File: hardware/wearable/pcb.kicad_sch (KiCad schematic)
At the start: 72 parts, among them IC1 LM4041CILPR, IC2 INA828IDR, IC3 MAX30102EFD+T, IC4 TPS63001DRCT, IC5 OPA2350UA, IC6 TPS62293DRVR, J1 Conn_02x05_Odd_Even, J2 Conn_01x04_Pin, SW1 SW_Push, SW2 SW_SPDT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

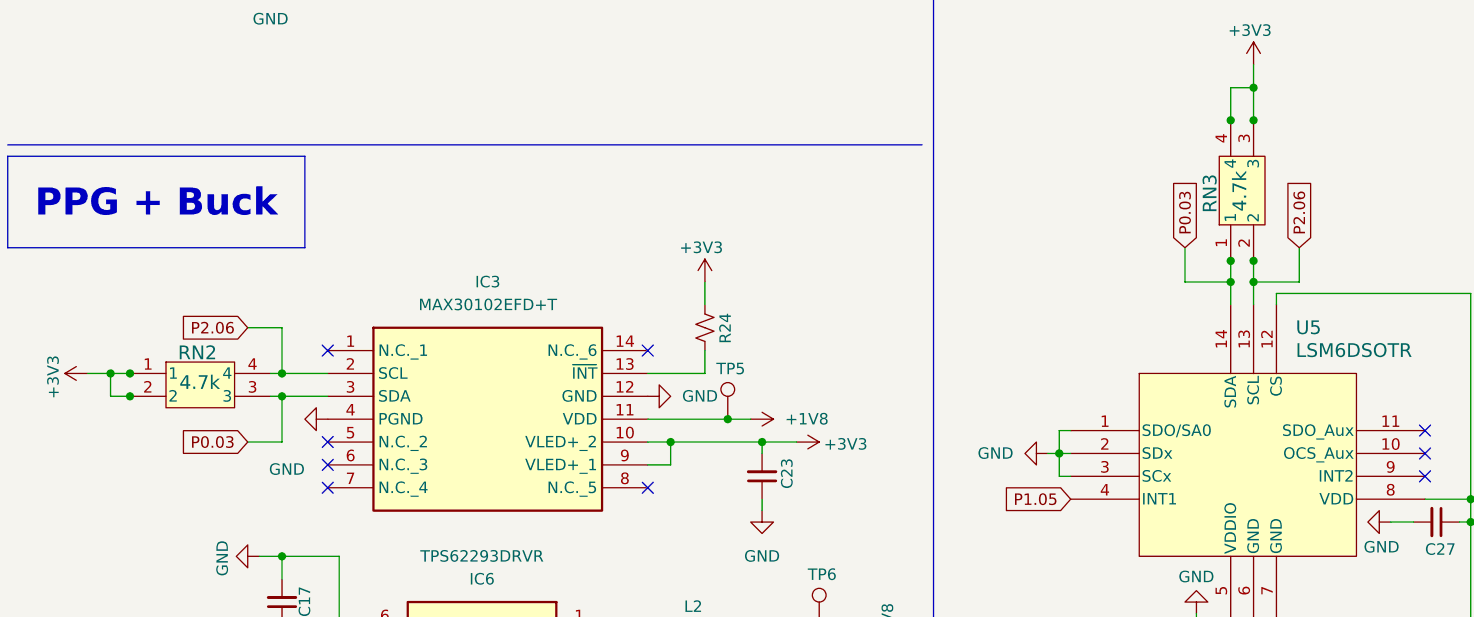
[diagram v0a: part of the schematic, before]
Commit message: ahhhhhhhhhhhhhhhhhhhhhhh firmware is no longer a submodule per peer request... thanks brianna...
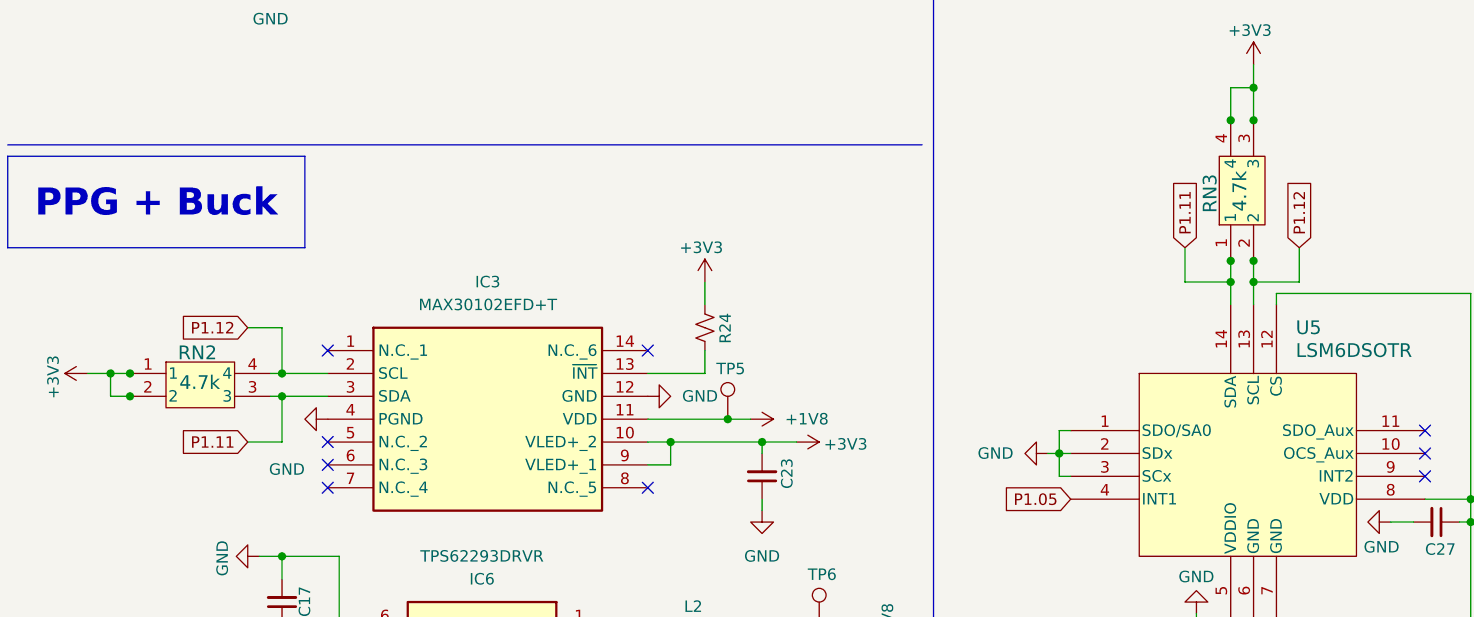
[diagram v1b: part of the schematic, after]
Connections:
- net P0.03: no longer IC3.3 (SDA), RN2.3, RN3.1, U5.14 (SDA)
- net P1.11: now also IC3.3 (SDA), RN2.3, RN3.1, U5.14 (SDA)
- net P1.12: now also IC3.2 (SCL), RN2.4, RN3.2, U5.13 (SCL)
- net P2.06: no longer IC3.2 (SCL), RN2.4, RN3.2, U5.13 (SCL)
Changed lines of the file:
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@@
 		)
 	)
-	(global_label "P2.06"
+	(global_label "P1.12"
 		(shape input)
 		(at 271.78 105.41 90)
@@
 		)
 	)
-	(global_label "P0.03"
+	(global_label "P1.11"
 		(shape input)
 		(at 259.08 105.41 90)
@@
 		)
 	)
-	(global_label "P2.06"
+	(global_label "P1.12"
 		(shape input)
 		(at 154.94 114.3 180)
@@
 		)
 	)
-	(global_label "P0.03"
+	(global_label "P1.11"
 		(shape input)
 		(at 154.94 127 180)
